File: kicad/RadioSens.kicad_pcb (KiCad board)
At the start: 2 copper layers, 62.6 x 42.7 mm, 200 parts, among them J1 Spacer M2, J2 Spacer M2, J3 Screw M2, J4 Screw M2, J5 Screw M2, J6 Screw M2

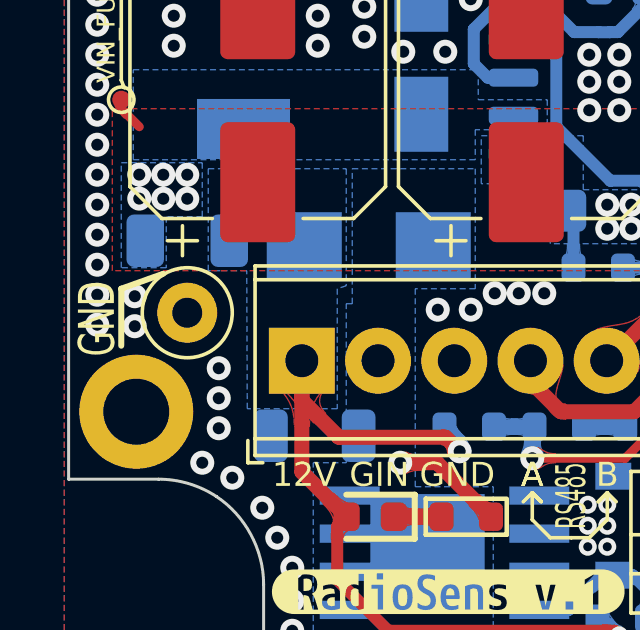
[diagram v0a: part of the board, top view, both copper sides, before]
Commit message: Add voltage value to caps, update BOM, SCH, ASM
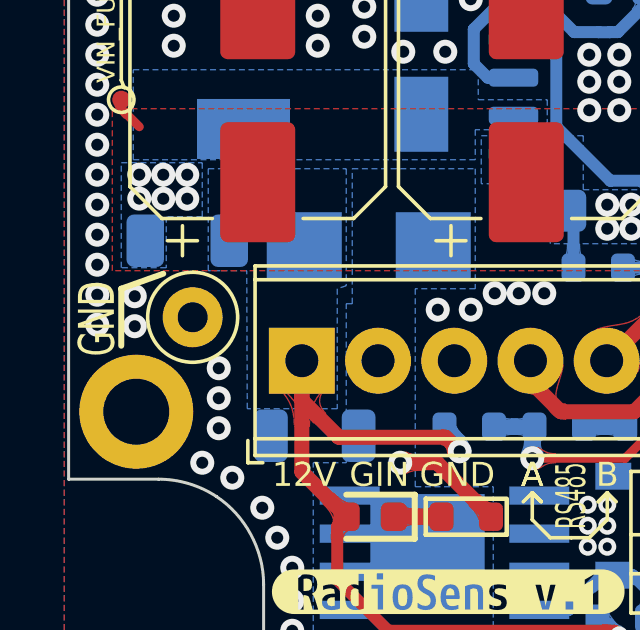
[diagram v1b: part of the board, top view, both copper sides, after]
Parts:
- removed XP1: Testpoint, TestPoint:TestPoint_Loop_D2.50mm_Drill1.0mm_LowProfile
- added XP9: Testpoint, TestPoint:TestPoint_Loop_D2.50mm_Drill1.0mm_LowProfile, F.Cu at (72.9, 109.1)
- C1, C30, C43, C45, C7, C9: value 1u -> 1u/25V
- C10, C11, C12, C13, C15, C19, C2, C22, C23, C24, C25, C36, C37, C40, C44, C6, C8: value 0.1u -> 0.1u/50V
- C14, C17: value 7 -> 7/50V
- C16, C18, C35, C41, C42: value 10u -> 10u/6.3V
- C20, C21: value 22 -> 22/50V
- C28: value 1u -> 1u/50V
- C29: value 3.3n -> 3.3n/50V
- C31, C32, C33, C34: value 100u -> 100u/6.3V
- C38: value 4.7u -> 4.7u/25V
- C39: value 0.22u -> 0.22u/50V
- C46: value 2.2u -> 2.2u/25V
- C5: value 10u -> 10u/16V
- J3, J4, J5, J6: value Screw M2 -> Spacer M2
- XT10, XT2, XT3, XT5, XT6, XT7, XT8: value XH2.54-3 -> NXW-03
- XT4: value XH2.54-2 -> NXW-02
